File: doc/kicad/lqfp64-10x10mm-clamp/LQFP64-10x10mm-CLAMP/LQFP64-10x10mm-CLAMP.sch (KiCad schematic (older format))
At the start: 11 parts, among them J0 Conn_01x01, J1 Conn_01x16, J2 Conn_01x16, J3 Conn_01x16, J4 Conn_01x16, J5 Conn_01x12, J6 Conn_01x12, J7 Conn_01x12, J8 Conn_01x12, U1 STM32F030RCTx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

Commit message: doc/kicad: add LQFP64-10x10mm-CLAMP
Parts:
- removed U1: STM32F030RCTx, Package_QFP:LQFP-64_10x10mm_P0.5mm, symbol MCU_ST_STM32F0:STM32F030RCTx
- removed U2: STM32F103C8Tx, Package_QFP:LQFP-48_7x7mm_P0.5mm, symbol MCU_ST_STM32F1:STM32F103C8Tx
- added U1: LQFP64-G, Package_QFP:LQFP-64_10x10mm_P0.5mm, symbol fmlibs:LQFP64-G
- added U2: LQFP48-G, Package_QFP:LQFP-48_7x7mm_P0.5mm, symbol fmlibs:LQFP48-G

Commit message: doc/kicad: LQFP64-10x10mm-CLAMP PCB layout (partly)
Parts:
- U1: footprint Package_QFP:LQFP-64_10x10mm_P0.5mm -> fmlibf:LQFP-64_10x10mm_P0.5mm_H
- U2: footprint Package_QFP:LQFP-48_7x7mm_P0.5mm -> fmlibf:LQFP-48_7x7mm_P0.5mm_H
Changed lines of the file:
@@
 F 0 "U1" H 2000 2150 50  0000 L CNN
 F 1 "LQFP64-G" H 1850 1950 50  0000 L CNN
-F 2 "Package_QFP:LQFP-64_10x10mm_P0.5mm" H 900 3050 50  0001 C CNN
+F 2 "fmlibf:LQFP-64_10x10mm_P0.5mm_H" H 900 3050 50  0001 C CNN
 F 3 "" H 900 3050 50  0001 C CNN
 	1    2050 2050
@@
 F 0 "U2" H 9600 1900 50  0000 L CNN
 F 1 "LQFP48-G" H 9450 1750 50  0000 L CNN
-F 2 "Package_QFP:LQFP-48_7x7mm_P0.5mm" H 8700 2650 50  0001 C CNN
+F 2 "fmlibf:LQFP-48_7x7mm_P0.5mm_H" H 8700 2650 50  0001 C CNN
 F 3 "" H 8700 2650 50  0001 C CNN
 	1    9650 1850

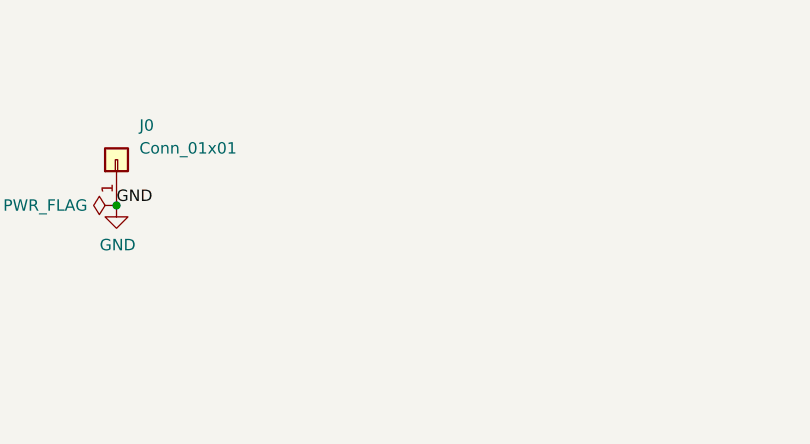
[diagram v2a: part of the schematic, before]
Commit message: doc/kicad: LQFP64-10x10mm-CLAMP bottom board
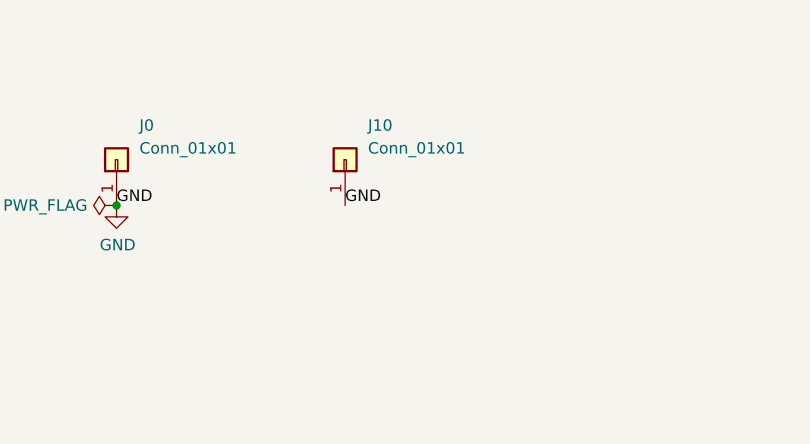
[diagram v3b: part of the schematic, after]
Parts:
- added J10: Conn_01x01, fmlibf:JS_2x2mm, symbol Connector_Generic:Conn_01x01
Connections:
- net GND: now also J10.1 (Pin_1)
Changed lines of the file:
@@
 	1    0    0    -1
 $EndComp
+$Comp
+L Connector_Generic:Conn_01x01 J10
+U 1 1 5FB0CC0B
+P 6500 1300
+F 0 "J10" V 6650 1200 50  0000 R CNN
+F 1 "Conn_01x01" V 6550 1200 50  0000 R CNN
+F 2 "fmlibf:JS_2x2mm" H 6500 1300 50  0001 C CNN
+F 3 "~" H 6500 1300 50  0001 C CNN
+	1    6500 1300
+	0    -1   -1   0
+$EndComp
+Text Label 6500 1500 0    50   ~ 0
+GND
 $EndSCHEMATC
